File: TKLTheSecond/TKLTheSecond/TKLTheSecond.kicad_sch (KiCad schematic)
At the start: 28 parts, among them J1 USB_C_Receptacle, J2 Conn_01x04_Socket, J3 Conn_01x02_Socket, SW62 SW_DIP_x01, SW63 SW_DIP_x01, SW64 SW_DIP_x01, U1 STM32F401RETx, U2 xc6206p332mr, Y1 25MHZ 9PF

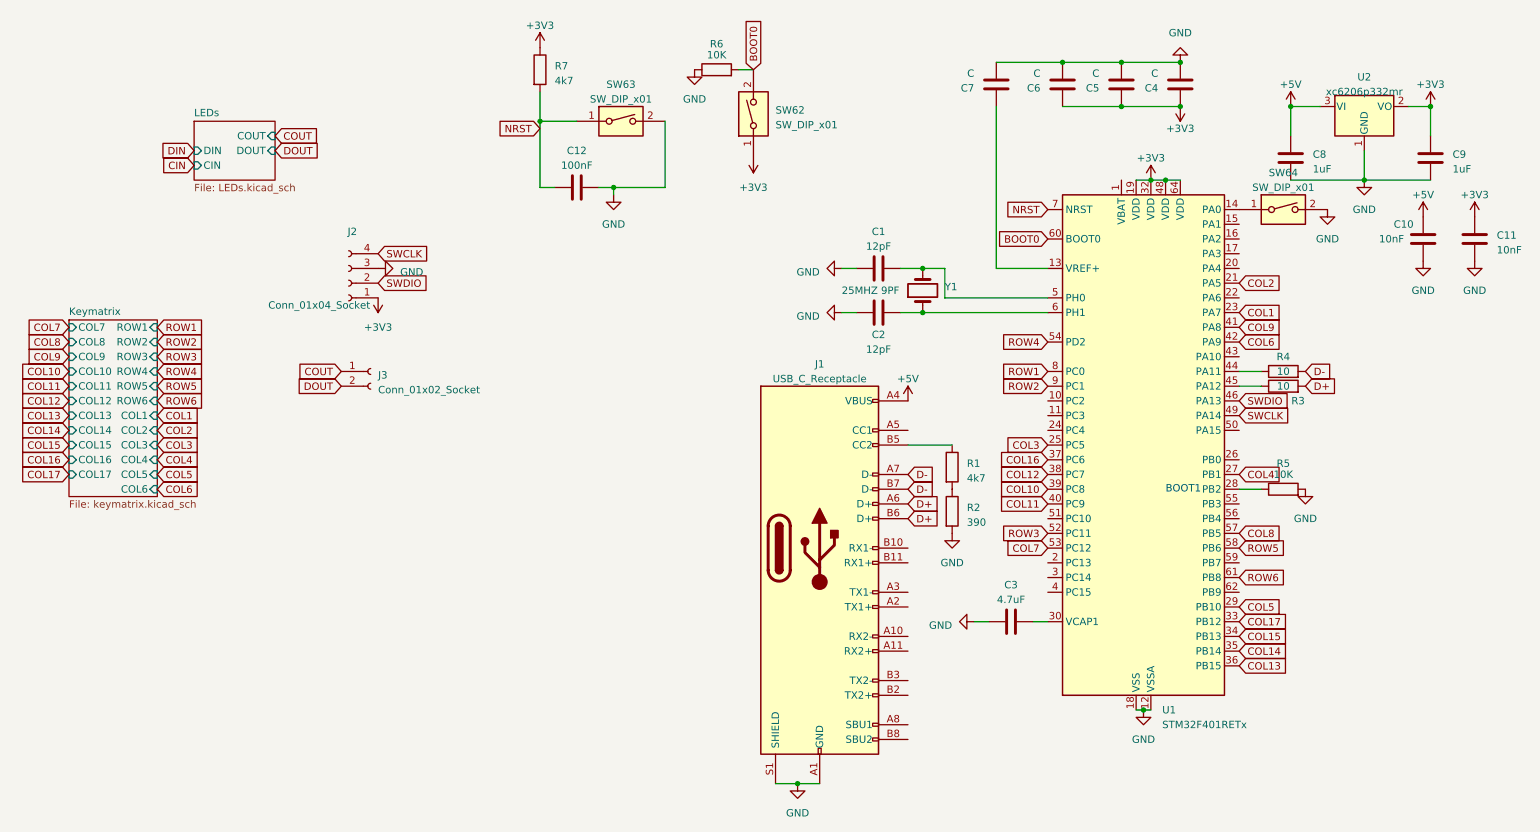
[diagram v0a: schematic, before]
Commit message: Started fixing MCU
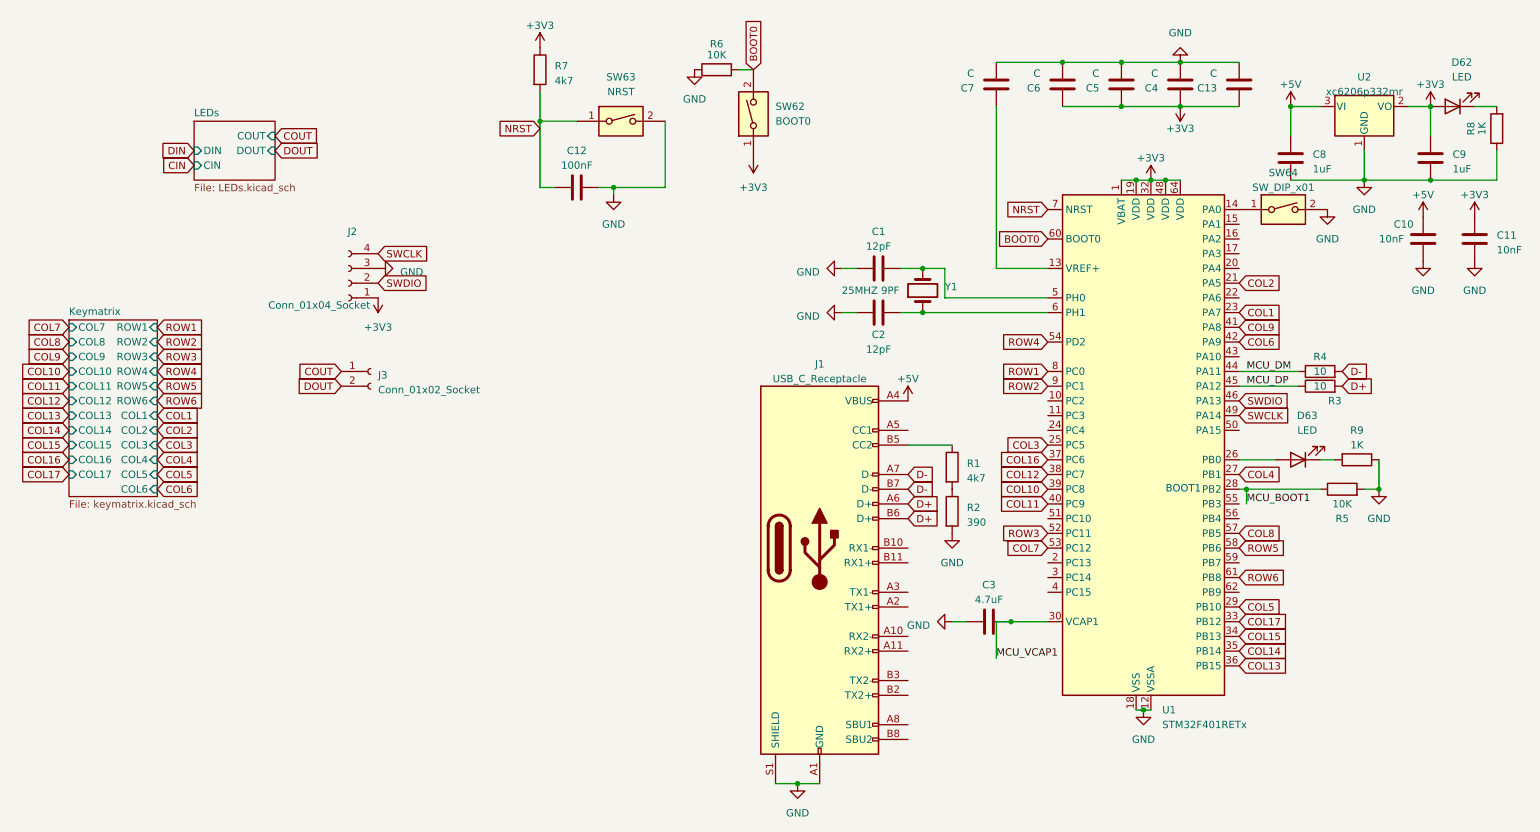
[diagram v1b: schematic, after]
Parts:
- added C13: C, Capacitor_SMD:C_1206_3216Metric, symbol Device:C
- added D62, D63: LED, LED_SMD:LED_1210_3225Metric_Pad1.42x2.65mm_HandSolder, symbol Device:LED
- added R8, R9: 1K, Resistor_SMD:R_1206_3216Metric, symbol PCM_Resistor_AKL:R_0201
- SW62: value SW_DIP_x01 -> BOOT0
- SW63: value SW_DIP_x01 -> NRST
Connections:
- net +3V3: now also U1.1 (VBAT), C13.1, D62.2 (A)
- net GND: now also C13.2, R8.1, R9.1
- net at U1.26 (PB0): now also D63.2 (A)
- net MCU_BOOT1: now reaches R5.1, U1.28 (PB2)
- net MCU_VCAP1: now reaches C3.2, U1.30 (VCAP1)
- net MCU_DM: now reaches R4.1, U1.44 (PA11)
- net MCU_DP: now reaches R3.1, U1.45 (PA12)
- new net: D63.1 (K), R9.2
- new net: D62.1 (K), R8.2
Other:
- moved on the sheet: C3, R3, R4, R5
